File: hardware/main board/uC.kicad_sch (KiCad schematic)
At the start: 28 parts, among them IC1 STM32WB55RGV6, Y1 8MHz

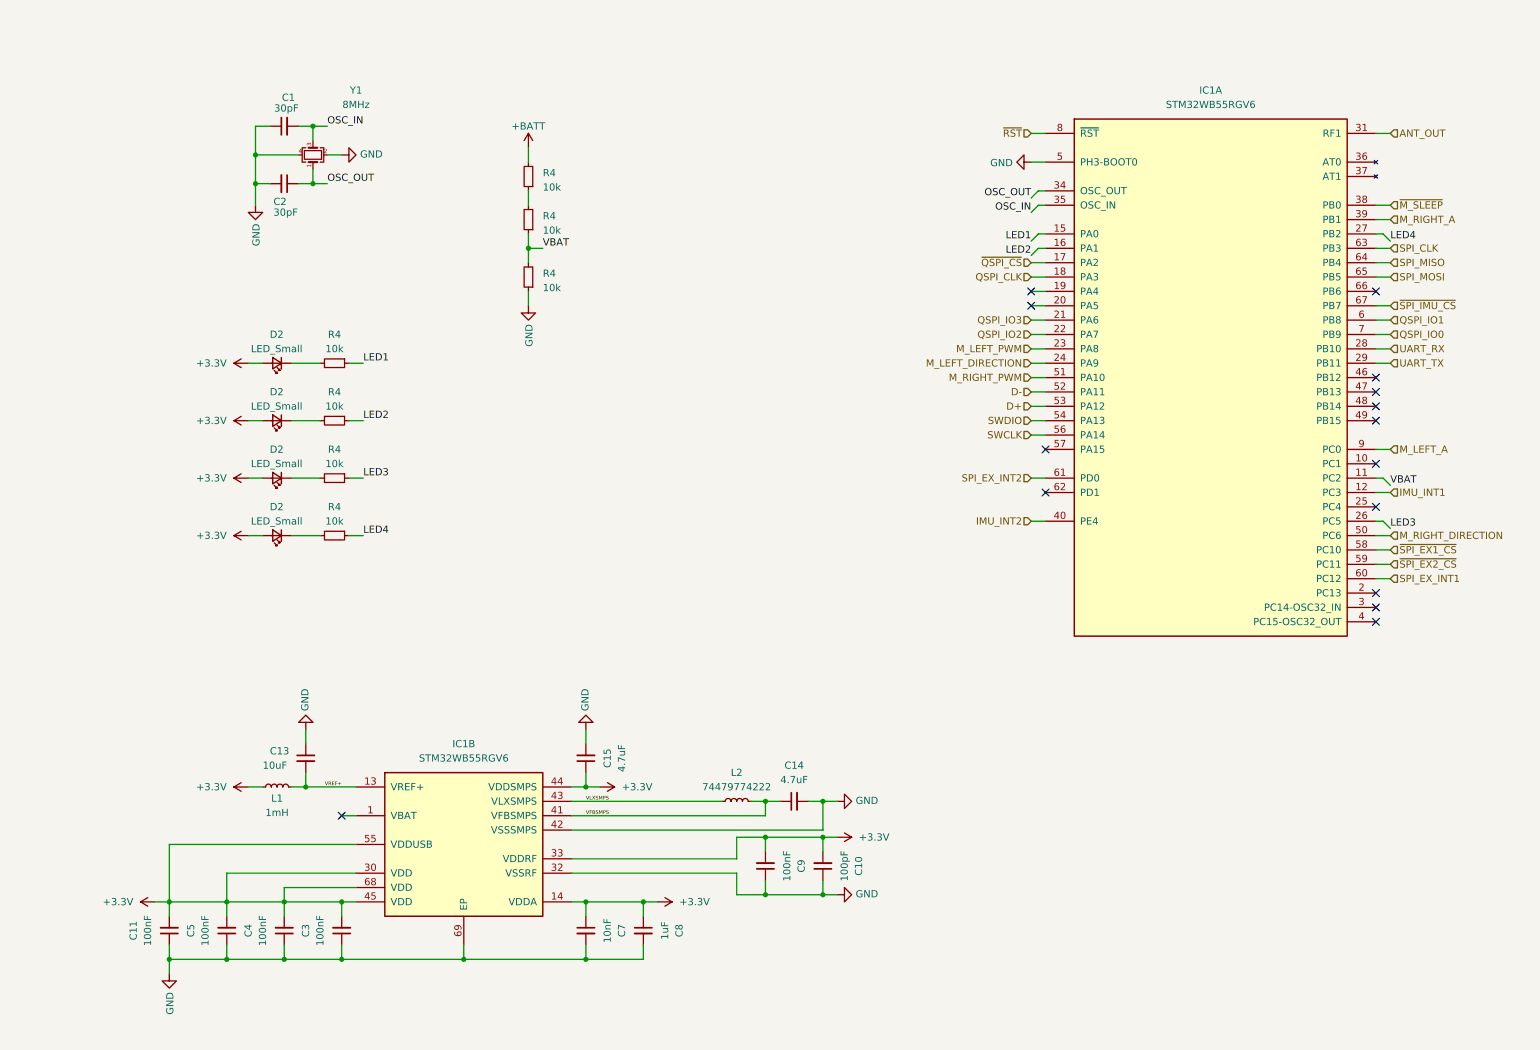
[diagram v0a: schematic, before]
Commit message: schematic changes to change it into a micro mouse
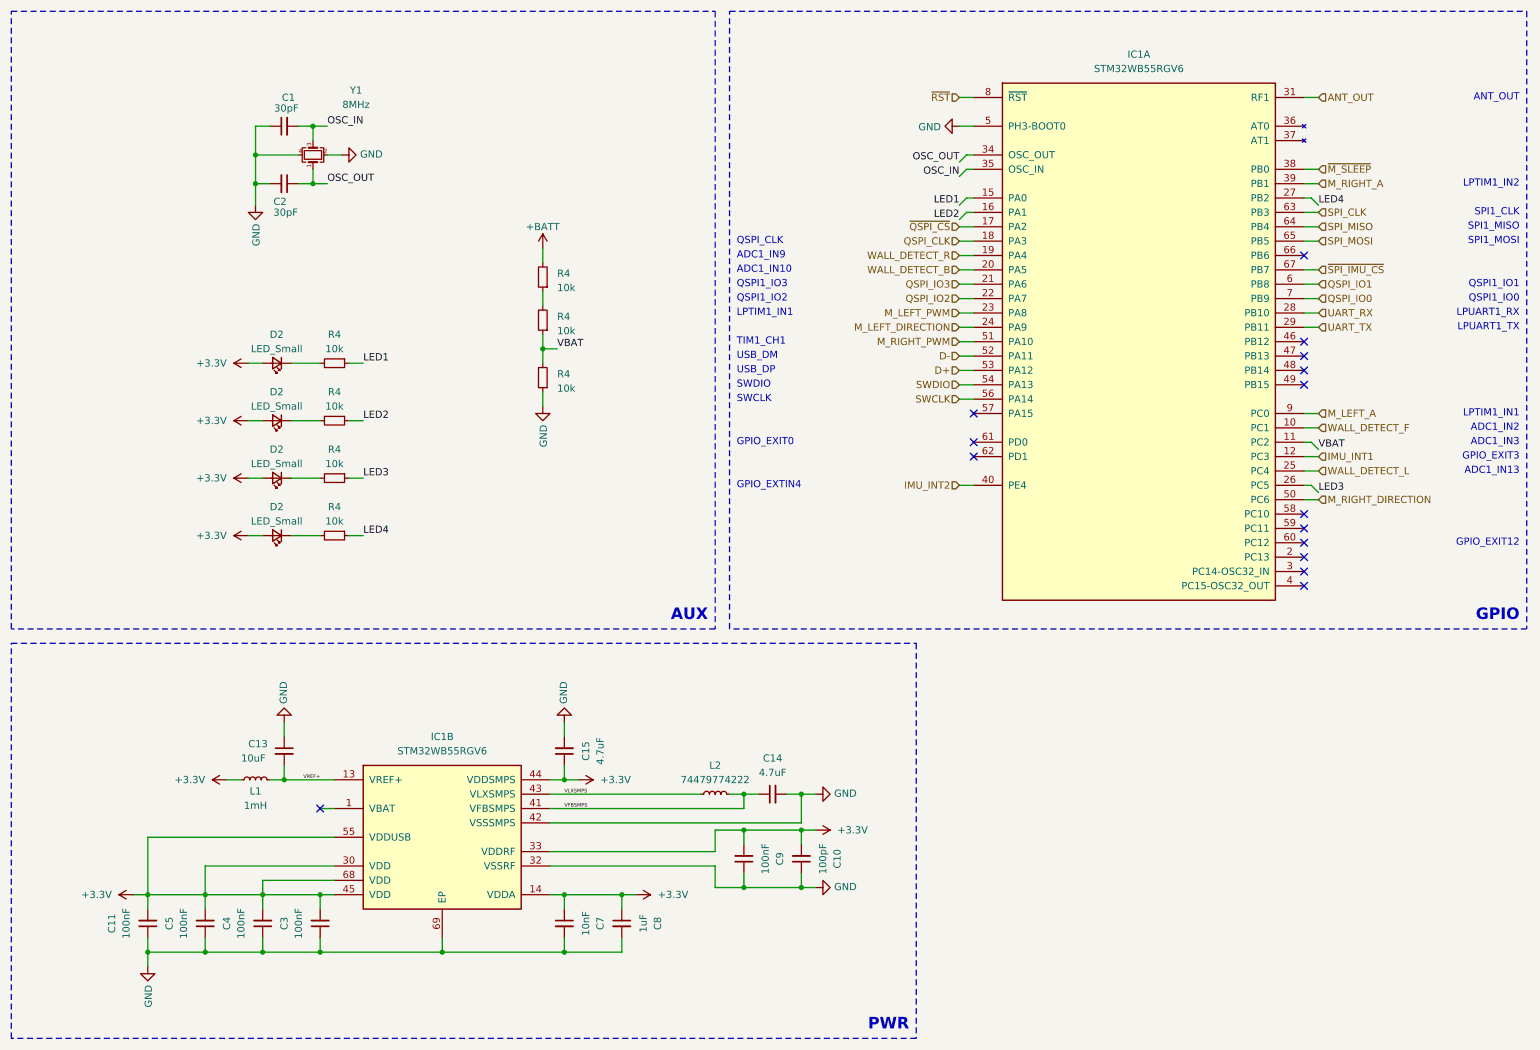
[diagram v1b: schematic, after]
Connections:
- net WALL_DETECT_F: now reaches IC1.10 (PC1)
- net WALL_DETECT_R: now reaches IC1.19 (PA4)
- net WALL_DETECT_B: now reaches IC1.20 (PA5)
- net WALL_DETECT_L: now reaches IC1.25 (PC4)
- net SPI_EX_INT1: no longer names the net of IC1.60 (PC12)
- net SPI_EX_INT2: no longer names the net of IC1.61 (PD0)
- net ~{SPI_EX1_CS}: no longer names the net of IC1.58 (PC10)
- net ~{SPI_EX2_CS}: no longer names the net of IC1.59 (PC11)
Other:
- note added: "ADC1_IN10"
- note added: "ADC1_IN13"
- note added: "ADC1_IN2"
- note added: "ADC1_IN3"
- note added: "ADC1_IN9"
- note added: "ANT_OUT"
- note added: "AUX"
- note added: "GPIO"
- note added: "GPIO_EXIT0"
- note added: "GPIO_EXIT12"
- note added: "GPIO_EXIT3"
- note added: "GPIO_EXTIN4"
- note added: "LPTIM1_IN1"
- note added: "LPTIM1_IN2"
- note added: "LPUART1_RX"
- note added: "LPUART1_TX"
- note added: "PWR"
- note added: "QSPI1_IO0"
- note added: "QSPI1_IO1"
- note added: "QSPI1_IO2"
- note added: "QSPI1_IO3"
- note added: "QSPI_CLK"
- note added: "SPI1_CLK"
- note added: "SPI1_MISO"
- note added: "SPI1_MOSI"
- note added: "SWCLK"
- note added: "SWDIO"
- note added: "TIM1_CH1"
- note added: "USB_DM"
- note added: "USB_DP"
- moved on the sheet: C10, C11, C13, C14, C15, C3, C4, C5, C7, C8, C9, IC1A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

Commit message: done
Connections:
- net WALL_DETECT_B: now also IC1.61 (PD0); no longer IC1.20 (PA5)
- net WALL_DETECT_F: now also IC1.59 (PC11); no longer IC1.10 (PC1)
- net WALL_DETECT_L: now also IC1.60 (PC12); no longer IC1.25 (PC4)
- net WALL_DETECT_R: now also IC1.58 (PC10); no longer IC1.19 (PA4)
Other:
- note removed: "ADC1_IN10"
- note removed: "ADC1_IN13"
- note removed: "ADC1_IN2"
- note removed: "ADC1_IN9"
- note removed: "GPIO_EXIT0"
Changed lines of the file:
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@@
+	)
+	(no_connect
+		(at 184.15 57.15)
 	)
 	(no_connect
@@
 	)
 	(no_connect
-		(at 242.57 107.95)
-	)
-	(no_connect
-		(at 242.57 105.41)
+		(at 242.57 87.63)
 	)
 	(no_connect
@@
 	)
 	(no_connect
+		(at 242.57 95.25)
+	)
+	(no_connect
 		(at 242.57 72.39)
 	)
@@
 	)
 	(no_connect
-		(at 184.15 90.17)
-	)
-	(no_connect
 		(at 242.57 77.47)
 	)
@@
 	)
 	(no_connect
-		(at 242.57 102.87)
-	)
-	(no_connect
 		(at 242.57 74.93)
 	)
@@
 		(at 68.58 154.94)
 	)
+	(no_connect
+		(at 184.15 59.69)
+	)
 	(wire
 		(pts
@@
 	(wire
 		(pts
-			(xy 181.61 59.69) (xy 184.15 59.69)
-		)
-		(stroke
-			(width 0)
-			(type default)
-		)
-	)
-	(wire
-		(pts
 			(xy 245.11 100.33) (xy 242.57 100.33)
 		)
@@
 	(wire
 		(pts
-			(xy 242.57 95.25) (xy 245.11 95.25)
+			(xy 184.15 90.17) (xy 181.61 90.17)
 		)
 		(stroke
@@
 	(wire
 		(pts
-			(xy 242.57 87.63) (xy 245.11 87.63)
+			(xy 242.57 107.95) (xy 245.11 107.95)
 		)
 		(stroke
@@
 	(wire
 		(pts
+			(xy 242.57 102.87) (xy 245.11 102.87)
+		)
+		(stroke
+			(width 0)
+			(type default)
+		)
+	)
+	(wire
+		(pts
 			(xy 63.5 96.52) (xy 68.58 96.52)
 		)
@@
 	(wire
 		(pts
-			(xy 181.61 57.15) (xy 184.15 57.15)
+			(xy 245.11 105.41) (xy 242.57 105.41)
 		)
 		(stroke
@@
 		)
 	)
-	(text "ADC1_IN9"
-		(exclude_from_sim no)
-		(at 142.24 57.15 0)
+	(text "LPTIM1_IN1"
+		(exclude_from_sim no)
+		(at 142.24 67.31 0)
 		(effects
 			(font
@@
 		)
 	)
-	(text "LPTIM1_IN1"
-		(exclude_from_sim no)
-		(at 142.24 67.31 0)
+	(text "QSPI1_IO3"
+		(exclude_from_sim no)
+		(at 142.24 62.23 0)
 		(effects
 			(font
@@
 			)
 			(justify left)
-		)
-	)
-	(text "QSPI1_IO3"
-		(exclude_from_sim no)
-		(at 142.24 62.23 0)
-		(effects
-			(font
-				(size 1.27 1.27)
-			)
-			(justify left)
-		)
-	)
-	(text "ADC1_IN2"
-		(exclude_from_sim no)
-		(at 280.67 87.63 0)
-		(effects
-			(font
-				(size 1.27 1.27)
-			)
-			(justify right)
 		)
 	)
@@
 		)
 	)
-	(text "ADC1_IN13"
-		(exclude_from_sim no)
-		(at 280.67 95.25 0)
-		(effects
-			(font
-				(size 1.27 1.27)
-			)
-			(justify right)
-		)
-	)
 	(text "PWR"
 		(exclude_from_sim no)
@@
 		)
 	)
-	(text "GPIO_EXIT0"
-		(exclude_from_sim no)
-		(at 142.24 90.17 0)
+	(text "LPTIM1_IN2"
+		(exclude_from_sim no)
+		(at 280.67 44.45 0)
+		(effects
+			(font
+				(size 1.27 1.27)
+			)
+			(justify right)
+		)
+	)
+	(text "GPIO_EXIT12"
+		(exclude_from_sim no)
+		(at 280.67 107.95 0)
+		(effects
+			(font
+				(size 1.27 1.27)
+			)
+			(justify right)
+		)
+	)
+	(text "SWDIO"
+		(exclude_from_sim no)
+		(at 142.24 80.01 0)
 		(effects
 			(font
@@
 		)
 	)
-	(text "LPTIM1_IN2"
-		(exclude_from_sim no)
-		(at 280.67 44.45 0)
-		(effects
-			(font
-				(size 1.27 1.27)
-			)
-			(justify right)
-		)
-	)
-	(text "GPIO_EXIT12"
-		(exclude_from_sim no)
-		(at 280.67 107.95 0)
-		(effects
-			(font
-				(size 1.27 1.27)
-			)
-			(justify right)
-		)
-	)
-	(text "SWDIO"
-		(exclude_from_sim no)
-		(at 142.24 80.01 0)
+	(text "QSPI1_IO0"
+		(exclude_from_sim no)
+		(at 280.67 64.77 0)
+		(effects
+			(font
+				(size 1.27 1.27)
+			)
+			(justify right)
+		)
+	)
+	(text "ANT_OUT"
+		(exclude_from_sim no)
+		(at 280.67 29.21 0)
+		(effects
+			(font
+				(size 1.27 1.27)
+			)
+			(justify right)
+		)
+	)
+	(text "QSPI1_IO2"
+		(exclude_from_sim no)
+		(at 142.24 64.77 0)
 		(effects
 			(font
@@
 		)
 	)
-	(text "QSPI1_IO0"
-		(exclude_from_sim no)
-		(at 280.67 64.77 0)
-		(effects
-			(font
-				(size 1.27 1.27)
-			)
-			(justify right)
-		)
-	)
-	(text "ANT_OUT"
-		(exclude_from_sim no)
-		(at 280.67 29.21 0)
-		(effects
-			(font
-				(size 1.27 1.27)
-			)
-			(justify right)
-		)
-	)
-	(text "QSPI1_IO2"
-		(exclude_from_sim no)
-		(at 142.24 64.77 0)
+	(text "SPI1_MOSI"
+		(exclude_from_sim no)
+		(at 280.67 54.61 0)
+		(effects
+			(font
+				(size 1.27 1.27)
+			)
+			(justify right)
+		)
+	)
+	(text "USB_DM"
+		(exclude_from_sim no)
+		(at 142.24 74.93 0)
 		(effects
 			(font
@@
 		)
 	)
-	(text "SPI1_MOSI"
-		(exclude_from_sim no)
-		(at 280.67 54.61 0)
-		(effects
-			(font
-				(size 1.27 1.27)
-			)
-			(justify right)
-		)
-	)
-	(text "USB_DM"
-		(exclude_from_sim no)
-		(at 142.24 74.93 0)
+	(text "TIM1_CH1"
+		(exclude_from_sim no)
+		(at 142.24 72.39 0)
 		(effects
 			(font
@@
 		)
 	)
-	(text "TIM1_CH1"
-		(exclude_from_sim no)
-		(at 142.24 72.39 0)
-		(effects
-			(font
-				(size 1.27 1.27)
-			)
-			(justify left)
-		)
-	)
 	(text "GPIO_EXTIN4"
 		(exclude_from_sim no)
 		(at 142.24 97.79 0)
-		(effects
-			(font
-				(size 1.27 1.27)
-			)
-			(justify left)
-		)
-	)
-	(text "ADC1_IN10"
-		(exclude_from_sim no)
-		(at 142.24 59.69 0)
 		(effects
 			(font
@@
 	(hierarchical_label "WALL_DETECT_R"
 		(shape input)
-		(at 181.61 57.15 180)
-		(fields_autoplaced yes)
-		(effects
-			(font
-				(size 1.27 1.27)
-			)
-			(justify right)
+		(at 245.11 102.87 0)
+		(fields_autoplaced yes)
+		(effects
+			(font
+				(size 1.27 1.27)
+			)
+			(justify left)
 		)
 	)
@@
 	(hierarchical_label "WALL_DETECT_B"
 		(shape input)
-		(at 181.61 59.69 180)
+		(at 181.61 90.17 180)
 		(fields_autoplaced yes)
 		(effects
@@
 	(hierarchical_label "WALL_DETECT_F"
 		(shape input)
-		(at 245.11 87.63 0)
+		(at 245.11 105.41 0)
 		(fields_autoplaced yes)
 		(effects
@@
 	(hierarchical_label "WALL_DETECT_L"
 		(shape input)
-		(at 245.11 95.25 0)
-		(fields_autoplaced yes)
-		(effects
+		(at 245.11 107.95 0)
+		(fields_autoplaced yes)
+		(effects

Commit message: final
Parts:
- D2: value LED_Small -> LED
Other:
- note removed: "GPIO_EXIT12"
- company: (none) -> Made by: Piotr Lesicki
- title: (none) -> Mirco Mouse
- moved on the sheet: C10, C11, C4, C5, C8
